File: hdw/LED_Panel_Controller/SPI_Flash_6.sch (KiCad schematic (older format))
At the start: 14 parts, among them U3001 74LVC1G97, U3002 SST25VF080B-50-4I-S2AF

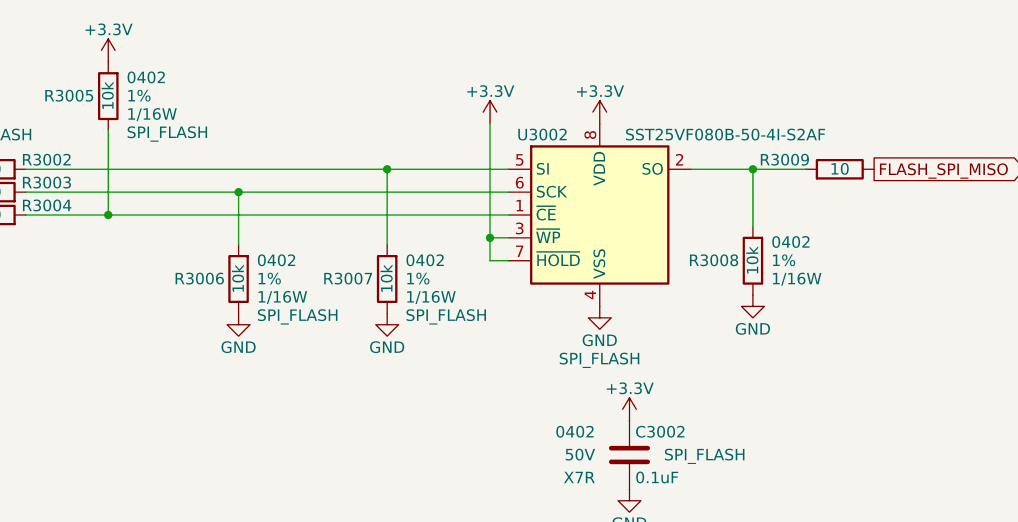
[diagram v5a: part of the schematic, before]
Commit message: fixed SPI flash pull resistors, more PCB placement
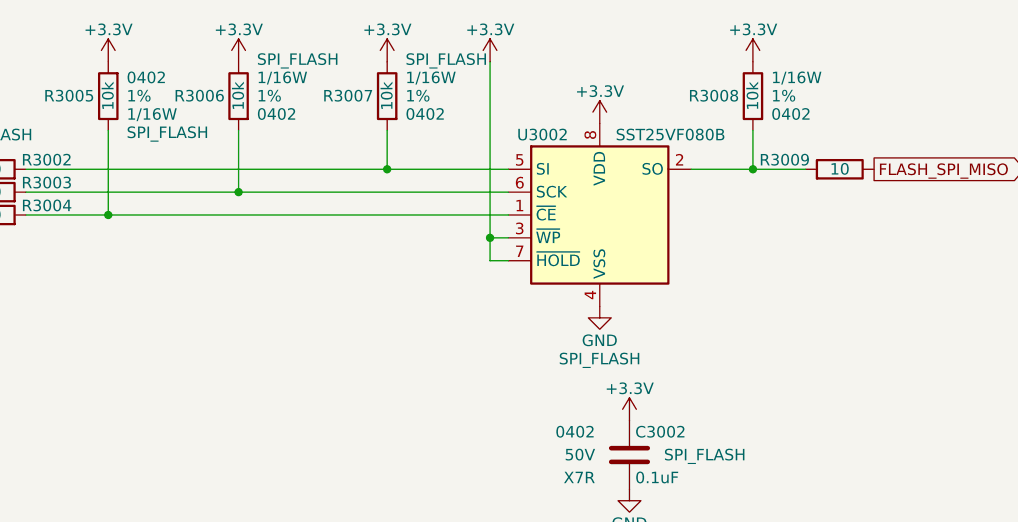
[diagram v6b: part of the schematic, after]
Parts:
- U3002: value SST25VF080B-50-4I-S2AF -> SST25VF080B
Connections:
- net +3V3: now also R3006.2, R3007.2, R3008.2
- net GND: no longer R3006.2, R3007.2, R3008.2
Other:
- moved on the sheet: R3006, R3007, R3008
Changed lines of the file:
@@
 L Custom_Library:R_Custom R3008
 U 1 1 60786264
-P 6750 3850
-F 0 "R3008" H 6690 3850 50  0000 R CNN
-F 1 "10k" V 6750 3850 50  0000 C CNN
-F 2 "Resistors_SMD:R_0402" H 6750 3850 50  0001 C CNN
-F 3 "" H 6750 3850 50  0001 C CNN
-F 4 "0402" H 6830 3930 50  0000 L CNN "display_footprint"
-F 5 "1%" H 6830 3850 50  0000 L CNN "Tolerance"
-F 6 "1/16W" H 6830 3770 50  0000 L CNN "Wattage"
-F 7 "RMCF0402FT10K0CT-ND" H 7050 4250 60  0001 C CNN "Digi-Key PN"
-	1    6750 3850
-	1    0    0    -1
-$EndComp
-$Comp
-L power:GND #PWR03008
-U 1 1 6078626B
-P 5150 4080
-F 0 "#PWR03008" H 5150 3830 50  0001 C CNN
-F 1 "GND" H 5150 3930 50  0000 C CNN
-F 2 "" H 5150 4080 50  0001 C CNN
-F 3 "" H 5150 4080 50  0001 C CNN
-	1    5150 4080
-	1    0    0    -1
-$EndComp
-$Comp
-L power:GND #PWR03014
-U 1 1 60786272
-P 6750 4000
-F 0 "#PWR03014" H 6750 3750 50  0001 C CNN
-F 1 "GND" H 6750 3850 50  0000 C CNN
-F 2 "" H 6750 4000 50  0001 C CNN
-F 3 "" H 6750 4000 50  0001 C CNN
-	1    6750 4000
-	1    0    0    -1
+P 6750 3130
+F 0 "R3008" H 6690 3130 50  0000 R CNN
+F 1 "10k" V 6750 3130 50  0000 C CNN
+F 2 "Resistors_SMD:R_0402" H 6750 3130 50  0001 C CNN
+F 3 "" H 6750 3130 50  0001 C CNN
+F 4 "0402" H 6830 3210 50  0000 L CNN "display_footprint"
+F 5 "1%" H 6830 3130 50  0000 L CNN "Tolerance"
+F 6 "1/16W" H 6830 3050 50  0000 L CNN "Wattage"
+F 7 "RMCF0402FT10K0CT-ND" H 7050 3530 60  0001 C CNN "Digi-Key PN"
+	1    6750 3130
+	1    0    0    1
 $EndComp
 $Comp
@@
 $EndComp
 Wire Wire Line
-	5150 3450 5150 3780
-Connection ~ 5150 3450
-Wire Wire Line
-	5150 3450 5680 3450
-Wire Wire Line
 	3930 3280 3930 3650
 Wire Wire Line
 	3930 3650 5680 3650
 Connection ~ 3930 3650
-Wire Wire Line
-	6980 3450 6750 3450
-Wire Wire Line
-	6750 3700 6750 3450
-Connection ~ 6750 3450
-Wire Wire Line
-	6750 3450 6480 3450
 Text GLabel 7280 3450 2    50   Output ~ 0
 FLASH_SPI_MISO
@@
 P 6080 3650
 F 0 "U3002" H 5830 4000 50  0000 C CNN
-F 1 "SST25VF080B-50-4I-S2AF" H 6630 4000 50  0000 C CNN
+F 1 "SST25VF080B" H 6630 4000 50  0000 R CNN
 F 2 "Package_SO:SOIC-8_5.275x5.275mm_P1.27mm" H 6080 2950 50  0001 C CNN
 F 3 "http://ww1.microchip.com/downloads/en/DeviceDoc/20005045C.pdf" H 6030 4200 50  0001 C CNN
@@
 L power:+3.3V #PWR03009
 U 1 1 6078630F
-P 5600 3250
-F 0 "#PWR03009" H 5600 3100 50  0001 C CNN
-F 1 "+3.3V" H 5600 3390 50  0000 C CNN
-F 2 "" H 5600 3250 50  0001 C CNN
-F 3 "" H 5600 3250 50  0001 C CNN
-	1    5600 3250
+P 5600 2980
+F 0 "#PWR03009" H 5600 2830 50  0001 C CNN
+F 1 "+3.3V" H 5600 3120 50  0000 C CNN
+F 2 "" H 5600 2980 50  0001 C CNN
+F 3 "" H 5600 2980 50  0001 C CNN
+	1    5600 2980
 	1    0    0    -1
 $EndComp
@@
 	5680 3750 5600 3750
 Wire Wire Line
-	5600 3750 5600 3250
+	5600 3750 5600 2980
 Wire Wire Line
 	5680 3850 5600 3850
@@
 	5600 3850 5600 3750
 Connection ~ 5600 3750
-Wire Wire Line
-	3570 3550 4500 3550
 $Comp
 L Custom_Library:R_Custom R3006
 U 1 1 60786313
-P 4500 3930
-F 0 "R3006" H 4440 3930 50  0000 R CNN
-F 1 "10k" V 4500 3930 50  0000 C CNN
-F 2 "Resistors_SMD:R_0402" H 4500 3930 50  0001 C CNN
-F 3 "" H 4500 3930 50  0001 C CNN
-F 4 "0402" H 4580 4010 50  0000 L CNN "display_footprint"
-F 5 "1%" H 4580 3930 50  0000 L CNN "Tolerance"
-F 6 "1/16W" H 4580 3850 50  0000 L CNN "Wattage"
-F 7 "RMCF0402FT10K0CT-ND" H 4800 4330 60  0001 C CNN "Digi-Key PN"
-F 8 "SPI_FLASH" H 4580 3770 50  0000 L CNN "Configuration"
-	1    4500 3930
-	1    0    0    -1
-$EndComp
-$Comp
-L power:GND #PWR03007
-U 1 1 6078631B
-P 4500 4080
-F 0 "#PWR03007" H 4500 3830 50  0001 C CNN
-F 1 "GND" H 4500 3930 50  0000 C CNN
-F 2 "" H 4500 4080 50  0001 C CNN
-F 3 "" H 4500 4080 50  0001 C CNN
-	1    4500 4080
-	1    0    0    -1
-$EndComp
-Wire Wire Line
-	3570 3450 5150 3450
-Wire Wire Line
-	4500 3550 4500 3780
-Connection ~ 4500 3550
-Wire Wire Line
-	4500 3550 5680 3550
+P 4500 3130
+F 0 "R3006" H 4440 3130 50  0000 R CNN
+F 1 "10k" V 4500 3130 50  0000 C CNN
+F 2 "Resistors_SMD:R_0402" H 4500 3130 50  0001 C CNN
+F 3 "" H 4500 3130 50  0001 C CNN
+F 4 "0402" H 4580 3210 50  0000 L CNN "display_footprint"
+F 5 "1%" H 4580 3130 50  0000 L CNN "Tolerance"
+F 6 "1/16W" H 4580 3050 50  0000 L CNN "Wattage"
+F 7 "RMCF0402FT10K0CT-ND" H 4800 3530 60  0001 C CNN "Digi-Key PN"
+F 8 "SPI_FLASH" H 4580 2970 50  0000 L CNN "Configuration"
+	1    4500 3130
+	1    0    0    1
+$EndComp
 $Comp
 L Custom_Library:R_Custom R3003
@@
 L Custom_Library:R_Custom R3007
 U 1 1 6078635B
-P 5150 3930
-F 0 "R3007" H 5090 3930 50  0000 R CNN
-F 1 "10k" V 5150 3930 50  0000 C CNN
-F 2 "Resistors_SMD:R_0402" H 5150 3930 50  0001 C CNN
-F 3 "" H 5150 3930 50  0001 C CNN
-F 4 "0402" H 5230 4010 50  0000 L CNN "display_footprint"
-F 5 "1%" H 5230 3930 50  0000 L CNN "Tolerance"
-F 6 "1/16W" H 5230 3850 50  0000 L CNN "Wattage"
-F 7 "RMCF0402FT10K0CT-ND" H 5450 4330 60  0001 C CNN "Digi-Key PN"
-F 8 "SPI_FLASH" H 5230 3770 50  0000 L CNN "Configuration"
-	1    5150 3930
-	1    0    0    -1
+P 5150 3130
+F 0 "R3007" H 5090 3130 50  0000 R CNN
+F 1 "10k" V 5150 3130 50  0000 C CNN
+F 2 "Resistors_SMD:R_0402" H 5150 3130 50  0001 C CNN
+F 3 "" H 5150 3130 50  0001 C CNN
+F 4 "0402" H 5230 3210 50  0000 L CNN "display_footprint"
+F 5 "1%" H 5230 3130 50  0000 L CNN "Tolerance"
+F 6 "1/16W" H 5230 3050 50  0000 L CNN "Wattage"
+F 7 "RMCF0402FT10K0CT-ND" H 5450 3530 60  0001 C CNN "Digi-Key PN"
+F 8 "SPI_FLASH" H 5230 2970 50  0000 L CNN "Configuration"
+	1    5150 3130
+	1    0    0    1
 $EndComp
 $Comp
@@
 	1    0    0    -1
 $EndComp
+Wire Wire Line
+	3570 3450 5150 3450
+Wire Wire Line
+	3570 3550 4500 3550
+$Comp
+L power:+3.3V #PWR0121
+U 1 1 6069B4F2
+P 4500 2980
+F 0 "#PWR0121" H 4500 2830 50  0001 C CNN
+F 1 "+3.3V" H 4500 3120 50  0000 C CNN
+F 2 "" H 4500 2980 50  0001 C CNN
+F 3 "" H 4500 2980 50  0001 C CNN
+	1    4500 2980
+	1    0    0    -1
+$EndComp
+$Comp
+L power:+3.3V #PWR0122
+U 1 1 6069B7D7
+P 5150 2980
+F 0 "#PWR0122" H 5150 2830 50  0001 C CNN
+F 1 "+3.3V" H 5150 3120 50  0000 C CNN
+F 2 "" H 5150 2980 50  0001 C CNN
+F 3 "" H 5150 2980 50  0001 C CNN
+	1    5150 2980
+	1    0    0    -1
+$EndComp
+Wire Wire Line
+	4500 3280 4500 3550
+Connection ~ 4500 3550
+Wire Wire Line
+	4500 3550 5680 3550
+Wire Wire Line
+	5150 3280 5150 3450
+Connection ~ 5150 3450
+Wire Wire Line
+	5150 3450 5680 3450
+Wire Wire Line
+	6480 3450 6750 3450
+Wire Wire Line
+	6750 3280 6750 3450
+Connection ~ 6750 3450
+Wire Wire Line
+	6750 3450 6980 3450
+$Comp
+L power:+3.3V #PWR0123
+U 1 1 6069CF02
+P 6750 2980
+F 0 "#PWR0123" H 6750 2830 50  0001 C CNN
+F 1 "+3.3V" H 6750 3120 50  0000 C CNN
+F 2 "" H 6750 2980 50  0001 C CNN
+F 3 "" H 6750 2980 50  0001 C CNN
+	1    6750 2980
+	1    0    0    -1
+$EndComp

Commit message: added BOMs, some consolidation
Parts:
- C3001, C3002: Digi-Key PN 490-10701-1-ND -> 490-10698-1-ND
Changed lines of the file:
@@
 F 5 "50V" H 1860 6900 50  0000 R CNN "Voltage"
 F 6 "X7R" H 1860 6800 50  0000 R CNN "Dielectric"
-F 7 "490-10701-1-ND" H 2435 7400 60  0001 C CNN "Digi-Key PN"
+F 7 "490-10698-1-ND" H 2435 7400 60  0001 C CNN "Digi-Key PN"
 F 8 "SPI_FLASH" H 2340 6900 50  0000 C CNN "Configuration"
 	1    2010 6900
@@
 F 5 "50V" H 6060 4700 50  0000 R CNN "Voltage"
 F 6 "X7R" H 6060 4600 50  0000 R CNN "Dielectric"
-F 7 "490-10701-1-ND" H 6635 5200 60  0001 C CNN "Digi-Key PN"
+F 7 "490-10698-1-ND" H 6635 5200 60  0001 C CNN "Digi-Key PN"
 F 8 "SPI_FLASH" H 6540 4700 50  0000 C CNN "Configuration"
 	1    6210 4700
